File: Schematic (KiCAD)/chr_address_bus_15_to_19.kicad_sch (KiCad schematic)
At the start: 85 parts

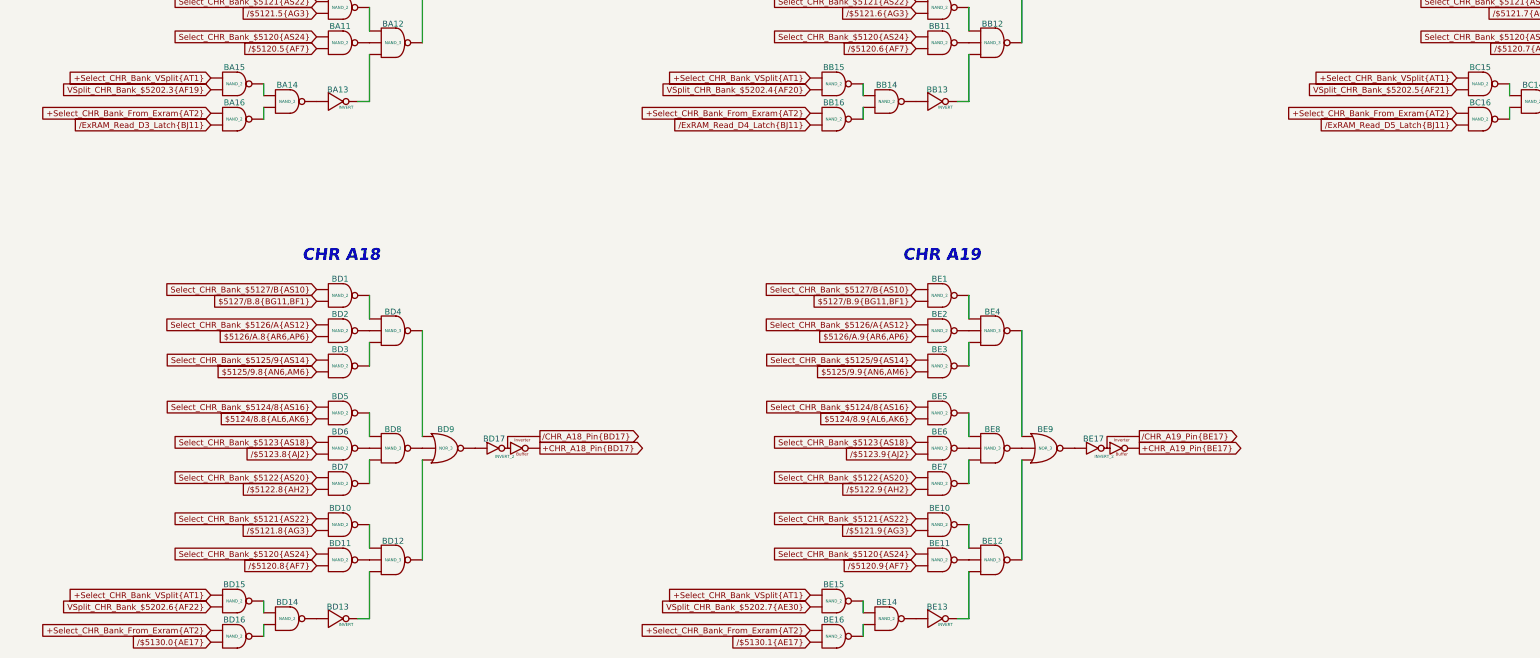
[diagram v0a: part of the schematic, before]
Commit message: - All cells in the left and center areas have now been added into the schematics.  - Changed naming of the PDF files; I was accidentally writing over furrtek's original with my new PDF.
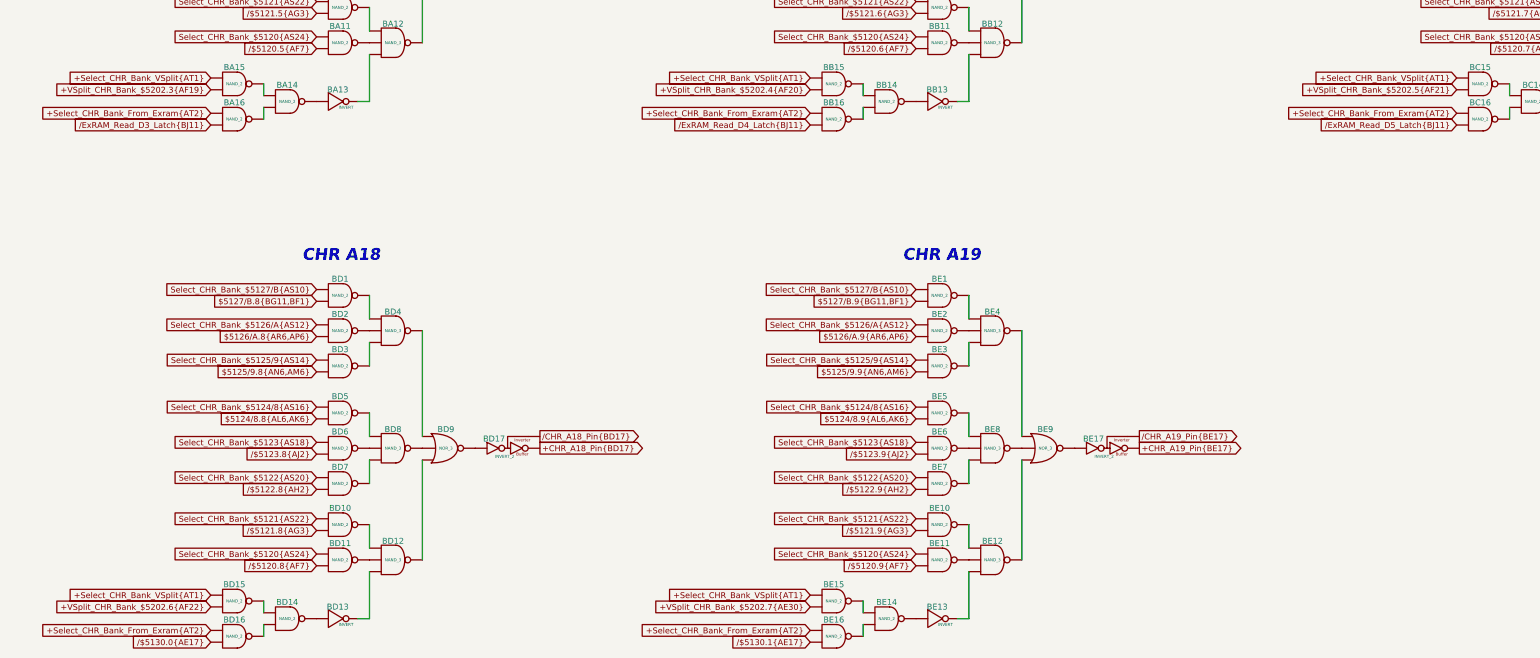
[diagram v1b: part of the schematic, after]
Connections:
- net VSplit_CHR_Bank_$5202.3{AF19} is gone; now on net +VSplit_CHR_Bank_$5202.3{AF19}: BA15. (X)
- net VSplit_CHR_Bank_$5202.4{AF20} is gone; now on net +VSplit_CHR_Bank_$5202.4{AF20}: BB15. (X)
- net VSplit_CHR_Bank_$5202.5{AF21} is gone; now on net +VSplit_CHR_Bank_$5202.5{AF21}: BC15. (X)
- net VSplit_CHR_Bank_$5202.6{AF22} is gone; now on net +VSplit_CHR_Bank_$5202.6{AF22}: BD15. (X)
- net VSplit_CHR_Bank_$5202.7{AE30} is gone; now on net +VSplit_CHR_Bank_$5202.7{AE30}: BE15. (X)
- net at BD9. (X): now also BD12. (X); no longer BD17. (X)
- net at BD8. (X): now also BD5. (X); no longer BD9. (X)
- net at BD4. (X): now also BD2. (X); no longer BD9. (X)
- net at BD12. (X): now also BD13. (X); no longer BD9. (X)
- net at BD14. (X): now also BD15. (X); no longer BD13. (X)
- net +VSplit_CHR_Bank_$5202.6{AF22}: now reaches BD15. (X)
- net +VSplit_CHR_Bank_$5202.6{AF22}: no longer BD14. (X)
- net at BC14. (X): now also BC15. (X); no longer BC16. (X)
- net at BC13. (X): now also BC12. (X); no longer BC14. (X)
- net at BC12. (X): now also BC11. (X); no longer BC13. (X)
- net at BB4. (X): now also BB1. (X); no longer BB3. (X)
- net at BC4. (X): now also BC3. (X); no longer BC2. (X)
- net at BA8. (X): now also BA9. (X); no longer BA6. (X)
- net at BE14. (X): now also BE15. (X); no longer BE16. (X)
- net at BE13. (X): now also BE12. (X); no longer BE14. (X)
- net +VSplit_CHR_Bank_$5202.7{AE30}: now reaches BE15. (X)
- net +VSplit_CHR_Bank_$5202.7{AE30}: no longer BE14. (X)
- net at BE8. (X): now also BE6. (X); no longer BE5. (X)
- net at BC9. (X): now also BC12. (X); no longer BC17. (X)
- net at BE4. (X): now also BE1. (X); no longer BE2. (X)
- net at BE9. (X): now also BE12. (X); no longer BE4. (X)
- net at BB8. (X): now also BB5. (X); no longer BB7. (X)
- net at BA12. (X): now also BA10. (X); no longer BA9. (X)
- net at BA13. (X): now also BA14. (X); no longer BA12. (X)
- net at BA9. (X): now also BA17. (X); no longer BA8. (X)
- net at BB12. (X): now also BB10. (X); no longer BB9. (X)
- net at BB13. (X): now also BB14. (X); no longer BB12. (X)
- net at BB9. (X): now also BB4. (X); no longer BB8. (X)
- net +VSplit_CHR_Bank_$5202.5{AF21}: now reaches BC15. (X)
- net +VSplit_CHR_Bank_$5202.5{AF21}: no longer BC14. (X)
- net +VSplit_CHR_Bank_$5202.4{AF20}: now reaches BB15. (X)
- net +VSplit_CHR_Bank_$5202.4{AF20}: no longer BB14. (X)
- net +VSplit_CHR_Bank_$5202.3{AF19}: now reaches BA15. (X)
- net +VSplit_CHR_Bank_$5202.3{AF19}: no longer BA14. (X)
- net at BA4. (X): now also BA2. (X); no longer BA3. (X)
- net at BC8. (X): now also BC7. (X); no longer BC5. (X)
- new net: BD17. (X), BD9. (X)
- new net: BD8. (X), BD9. (X)
- new net: BD4. (X), BD9. (X)
- new net: BD13. (X), BD14. (X)
- new net: BD14. (X), BD16. (X)
- new net: BC14. (X), BC16. (X)
- new net: BC13. (X), BC14. (X)
- new net: BB3. (X), BB4. (X)
- new net: BC2. (X), BC4. (X)
- new net: BD3. (X), BD4. (X)
- new net: BA6. (X), BA8. (X)
- new net: BD7. (X), BD8. (X)
- new net: BA5. (X), BA8. (X)
- new net: BE14. (X), BE16. (X)
- new net: BE13. (X), BE14. (X)
- new net: BE5. (X), BE8. (X)
- new net: BC17. (X), BC9. (X)
- new net: BE2. (X), BE4. (X)
- new net: BE4. (X), BE9. (X)
- new net: BE3. (X), BE4. (X)
- new net: BB7. (X), BB8. (X)
- new net: BB2. (X), BB4. (X)
- new net: BA12. (X), BA9. (X)
- new net: BA11. (X), BA12. (X)
- new net: BA12. (X), BA13. (X)
- new net: BD1. (X), BD4. (X)
- new net: BD11. (X), BD12. (X)
- new net: BA7. (X), BA8. (X)
- new net: BB12. (X), BB9. (X)
- new net: BB12. (X), BB13. (X)
- new net: BB11. (X), BB12. (X)
- new net: BC10. (X), BC12. (X)
- new net: BB8. (X), BB9. (X)
- new net: BB17. (X), BB9. (X)
- new net: BB14. (X), BB15. (X)
- new net: BB14. (X), BB16. (X)
- new net: BB6. (X), BB8. (X)
- new net: BD10. (X), BD12. (X)
- new net: BD6. (X), BD8. (X)
- new net: BA14. (X), BA15. (X)
- new net: BA14. (X), BA16. (X)
- new net: BA3. (X), BA4. (X)
- new net: BC5. (X), BC8. (X)
- new net: BC8. (X), BC9. (X)
- new net: BC4. (X), BC9. (X)
- new net: BA4. (X), BA9. (X)
- new net: BA1. (X), BA4. (X)
- new net: BC6. (X), BC8. (X)
- new net: BE11. (X), BE12. (X)
- new net: BE8. (X), BE9. (X)
- new net: BE7. (X), BE8. (X)
- new net: BC1. (X), BC4. (X)
- new net: BE10. (X), BE12. (X)
- new net: BE17. (X), BE9. (X)
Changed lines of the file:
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@@
 		)
 	)
-	(global_label "VSplit_CHR_Bank_$5202.3{AF19}"
+	(global_label "+VSplit_CHR_Bank_$5202.3{AF19}"
 		(shape input)
 		(at 52.07 99.06 180)
@@
 		)
 		(property "Intersheetrefs" "${INTERSHEET_REFS}"
-			(at 18.1212 99.06 0)
+			(at 16.5488 99.06 0)
 			(effects
 				(font
@@
 		)
 	)
-	(global_label "VSplit_CHR_Bank_$5202.4{AF20}"
+	(global_label "+VSplit_CHR_Bank_$5202.4{AF20}"
 		(shape input)
 		(at 181.61 99.06 180)
@@
 		)
 		(property "Intersheetrefs" "${INTERSHEET_REFS}"
-			(at 147.6612 99.06 0)
+			(at 146.0888 99.06 0)
 			(effects
 				(font
@@
 		)
 	)
-	(global_label "VSplit_CHR_Bank_$5202.7{AE30}"
+	(global_label "+VSplit_CHR_Bank_$5202.7{AE30}"
 		(shape input)
 		(at 181.61 210.82 180)
@@
 		)
 		(property "Intersheetrefs" "${INTERSHEET_REFS}"
-			(at 147.6008 210.82 0)
+			(at 146.0284 210.82 0)
 			(effects
 				(font
@@
 		)
 	)
-	(global_label "VSplit_CHR_Bank_$5202.6{AF22}"
+	(global_label "+VSplit_CHR_Bank_$5202.6{AF22}"
 		(shape input)
 		(at 52.07 210.82 180)
@@
 		)
 		(property "Intersheetrefs" "${INTERSHEET_REFS}"
-			(at 18.1212 210.82 0)
+			(at 16.5488 210.82 0)
 			(effects
 				(font
@@
 		)
 	)
-	(global_label "VSplit_CHR_Bank_$5202.5{AF21}"
+	(global_label "+VSplit_CHR_Bank_$5202.5{AF21}"
 		(shape input)
 		(at 321.31 99.06 180)
@@
 		)
 		(property "Intersheetrefs" "${INTERSHEET_REFS}"
-			(at 287.3612 99.06 0)
-			(effects
-				(font
+			(at 285.7888 99.06 0)
+			(effects
+				(font

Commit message: - All known gates and traces are now accounted for in the schematics!  :)
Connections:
- net at BD9. (X): now also BD12. (X); no longer BD17. (X)
- net at BD8. (X): now also BD5. (X); no longer BD9. (X)
- net at BD4. (X): now also BD2. (X); no longer BD9. (X)
- net at BD12. (X): now also BD13. (X); no longer BD9. (X)
- net at BD14. (X): now also BD15. (X); no longer BD13. (X)
- net at BC14. (X): now also BC15. (X); no longer BC16. (X)
- net at BC13. (X): now also BC12. (X); no longer BC14. (X)
- net at BC12. (X): now also BC11. (X); no longer BC13. (X)
- net at BB4. (X): now also BB1. (X); no longer BB3. (X)
- net at BC4. (X): now also BC3. (X); no longer BC2. (X)
- net at BA8. (X): now also BA9. (X); no longer BA6. (X)
- net at BE14. (X): now also BE15. (X); no longer BE16. (X)
- net at BE13. (X): now also BE12. (X); no longer BE14. (X)
- net at BE8. (X): now also BE6. (X); no longer BE5. (X)
- net at BC9. (X): now also BC12. (X); no longer BC17. (X)
- net at BE4. (X): now also BE1. (X); no longer BE2. (X)
- net at BE9. (X): now also BE12. (X); no longer BE4. (X)
- net at BB8. (X): now also BB5. (X); no longer BB7. (X)
- net at BA12. (X): now also BA10. (X); no longer BA9. (X)
- net at BA13. (X): now also BA14. (X); no longer BA12. (X)
- net at BA9. (X): now also BA17. (X); no longer BA8. (X)
- net at BB12. (X): now also BB10. (X); no longer BB9. (X)
- net at BB13. (X): now also BB14. (X); no longer BB12. (X)
- net at BB9. (X): now also BB4. (X); no longer BB8. (X)
- net at BA4. (X): now also BA2. (X); no longer BA3. (X)
- net at BC8. (X): now also BC7. (X); no longer BC5. (X)
- new net: BD17. (X), BD9. (X)
- new net: BD8. (X), BD9. (X)
- new net: BD4. (X), BD9. (X)
- new net: BD13. (X), BD14. (X)
- new net: BD14. (X), BD16. (X)
- new net: BC14. (X), BC16. (X)
- new net: BC13. (X), BC14. (X)
- new net: BB3. (X), BB4. (X)
- new net: BC2. (X), BC4. (X)
- new net: BD3. (X), BD4. (X)
- new net: BA6. (X), BA8. (X)
- new net: BD7. (X), BD8. (X)
- new net: BA5. (X), BA8. (X)
- new net: BE14. (X), BE16. (X)
- new net: BE13. (X), BE14. (X)
- new net: BE5. (X), BE8. (X)
- new net: BC17. (X), BC9. (X)
- new net: BE2. (X), BE4. (X)
- new net: BE4. (X), BE9. (X)
- new net: BE3. (X), BE4. (X)
- new net: BB7. (X), BB8. (X)
- new net: BB2. (X), BB4. (X)
- new net: BA12. (X), BA9. (X)
- new net: BA11. (X), BA12. (X)
- new net: BA12. (X), BA13. (X)
- new net: BD1. (X), BD4. (X)
- new net: BD11. (X), BD12. (X)
- new net: BA7. (X), BA8. (X)
- new net: BB12. (X), BB9. (X)
- new net: BB12. (X), BB13. (X)
- new net: BB11. (X), BB12. (X)
- new net: BC10. (X), BC12. (X)
- new net: BB8. (X), BB9. (X)
- new net: BB17. (X), BB9. (X)
- new net: BB14. (X), BB15. (X)
- new net: BB14. (X), BB16. (X)
- new net: BB6. (X), BB8. (X)
- new net: BD10. (X), BD12. (X)
- new net: BD6. (X), BD8. (X)
- new net: BA14. (X), BA15. (X)
- new net: BA14. (X), BA16. (X)
- new net: BA3. (X), BA4. (X)
- new net: BC5. (X), BC8. (X)
- new net: BC8. (X), BC9. (X)
- new net: BC4. (X), BC9. (X)
- new net: BA4. (X), BA9. (X)
- new net: BA1. (X), BA4. (X)
- new net: BC6. (X), BC8. (X)
- new net: BE11. (X), BE12. (X)
- new net: BE8. (X), BE9. (X)
- new net: BE7. (X), BE8. (X)
- new net: BC1. (X), BC4. (X)
- new net: BE10. (X), BE12. (X)
- new net: BE17. (X), BE9. (X)
